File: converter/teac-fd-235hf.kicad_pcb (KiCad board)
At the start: 2 copper layers, 92.1 x 21 mm, 9 parts, among them J1 P7X Side, J2 Drive Side, J3 Floppy Power

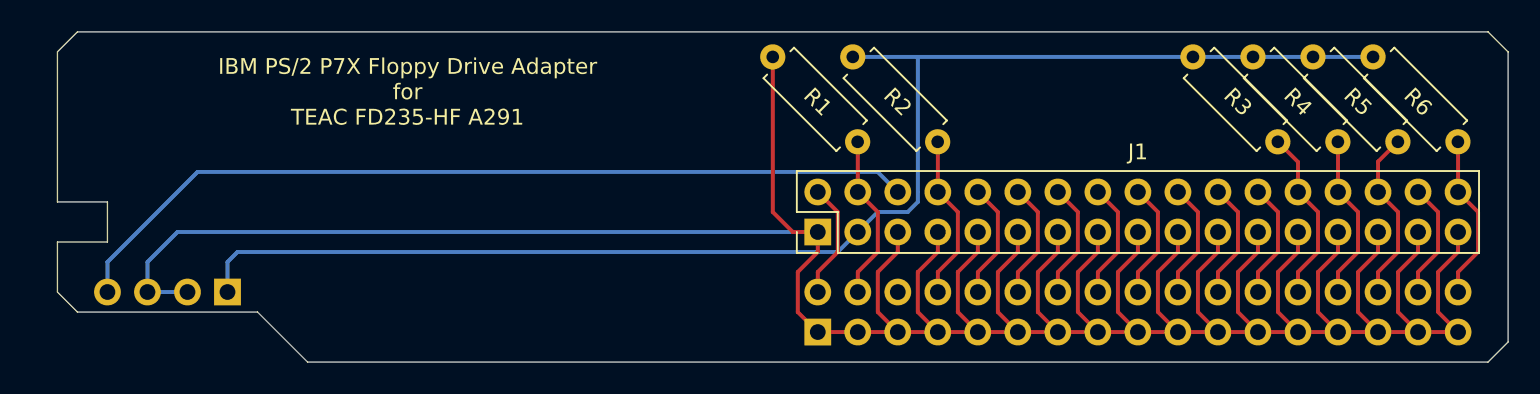
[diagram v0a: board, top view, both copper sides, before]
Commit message: Adjust for TEAC FD-235HF-6291
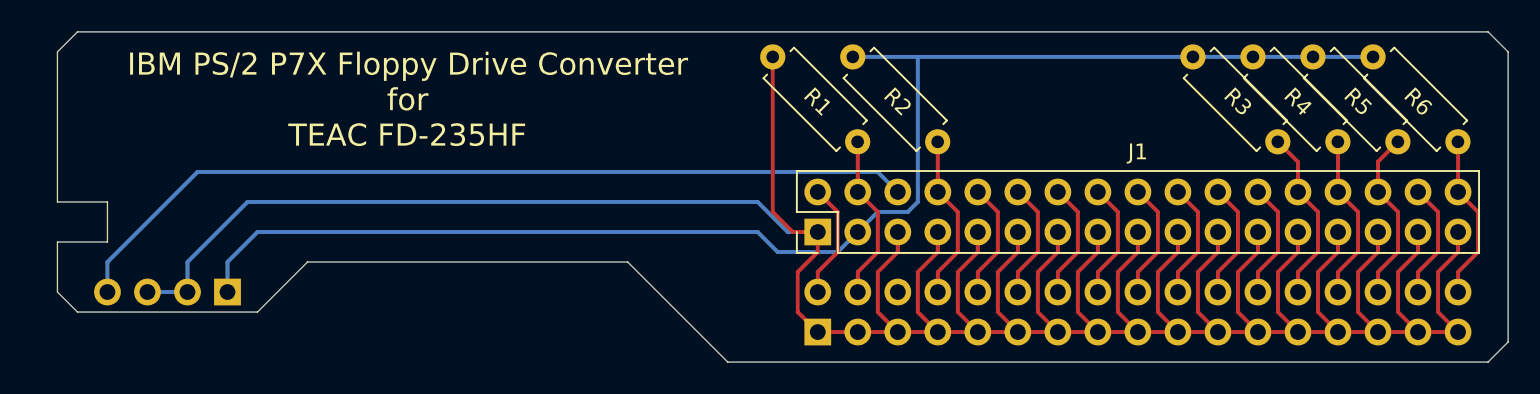
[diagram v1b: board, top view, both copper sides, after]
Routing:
- net +5V: track 89.5 -> 90.6 mm
- net GND: track 220.1 -> 219.1 mm
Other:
- outline, holes or cut-outs redrawn
- board text added: "IBM PS/2 P7X Floppy Drive Converter for TEAC FD-235HF"
- board text removed: "IBM PS/2 P7X Floppy Drive Adapter for TEAC FD235-HF A291"
